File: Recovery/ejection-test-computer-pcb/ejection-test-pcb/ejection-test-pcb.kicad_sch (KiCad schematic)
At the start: 21 parts, among them J1 BATTERY_TERMINAL, J2 LOAD_CELL_CONNECTOR, J3 NICHROME-TERMINAL, Q1 IRLZ34N, SW1 ON, U1 HX7111, U2 LM2596, U3 ESP32_DEVKIT

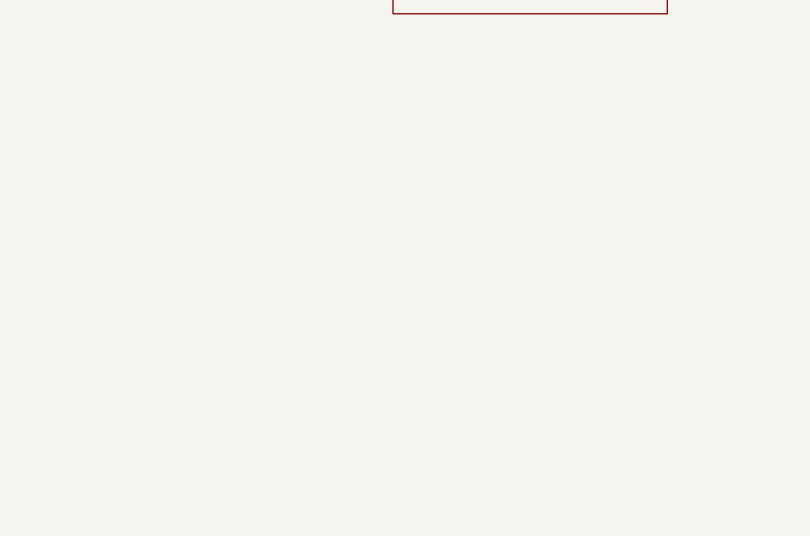
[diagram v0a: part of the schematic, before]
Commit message: added websocket
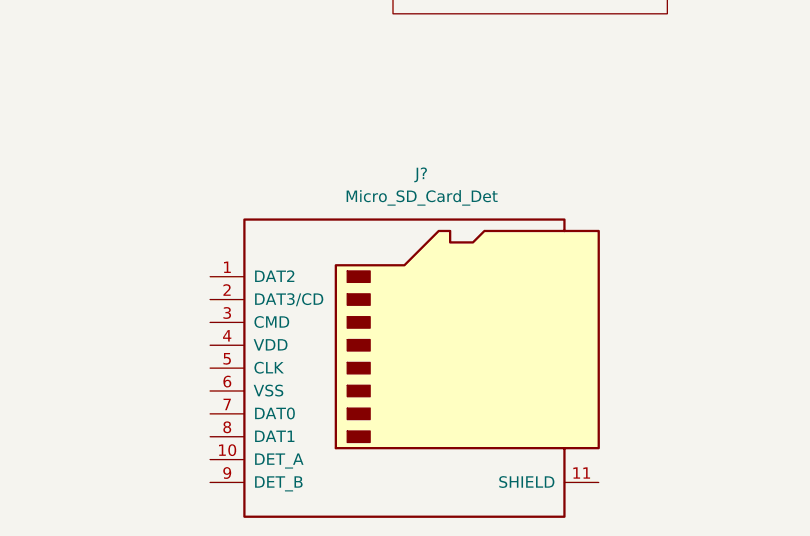
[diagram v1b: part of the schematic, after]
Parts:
- added J?: Micro_SD_Card_Det, symbol Connector:Micro_SD_Card_Det
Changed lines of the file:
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@@
     )
+  )
+  (symbol (lib_id "Connector:Micro_SD_Card_Det") (at 142.24 173.99 0) (unit 1)
+    (in_bom yes) (on_board yes) (fields_autoplaced)
+    (property "Reference" "J?" (id 0) (at 142.875 152.4 0))
+    (property "Value" "Micro_SD_Card_Det" (id 1) (at 142.875 154.94 0))
+    (property "Footprint" "" (id 2) (at 194.31 156.21 0)
+      (effects (font (size 1.27 1.27)) hide)
+    )
+    (property "Datasheet" "https://www.hirose.com/product/en/download_file/key_name/DM3/category/Catalog/doc_file_id/49662/?file_category_id=4&item_id=195&is_series=1" (id 3) (at 142.24 171.45 0)
+      (effects (font (size 1.27 1.27)) hide)
+    )
+    (pin "1")
+    (pin "10")
+    (pin "11")
+    (pin "2")
+    (pin "3")
+    (pin "4")
+    (pin "5")
+    (pin "6")
+    (pin "7")
+    (pin "8")
+    (pin "9")
   )
   (symbol (lib_id "power:GND") (at 195.58 62.23 0) (unit 1)
@@
       (reference "J3") (unit 1) (value "NICHROME-TERMINAL") (footprint "TerminalBlock:TerminalBlock_bornier-2_P5.08mm")
     )
+    (path "/ab348d08-997e-4cc6-a582-90b9e2626bcc"
+      (reference "J?") (unit 1) (value "Micro_SD_Card_Det") (footprint "")
+    )
     (path "/5b7189bd-e7fc-4d66-b9af-d65b01750a9c"
